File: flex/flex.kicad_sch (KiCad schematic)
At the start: 6 parts, among them SW1 SW_Push, SW2 SW_Push, SW3 SW_Push

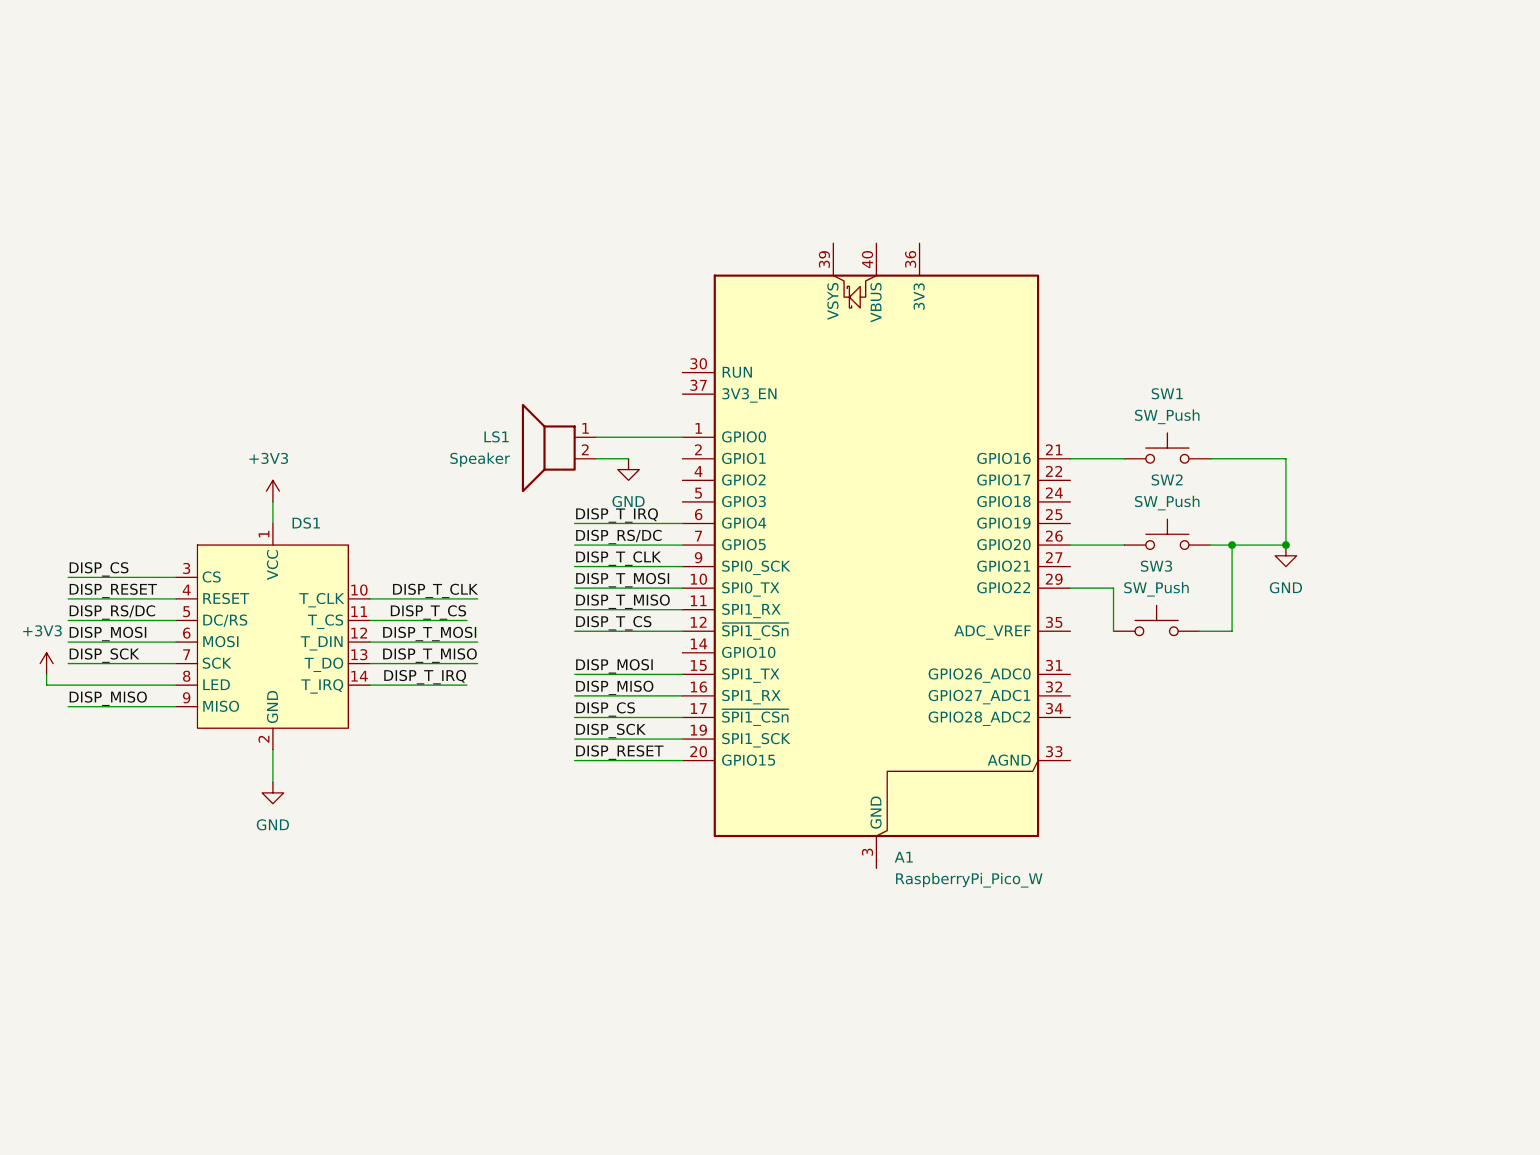
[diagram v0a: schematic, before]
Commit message: added 3d models and moved buttons and edge
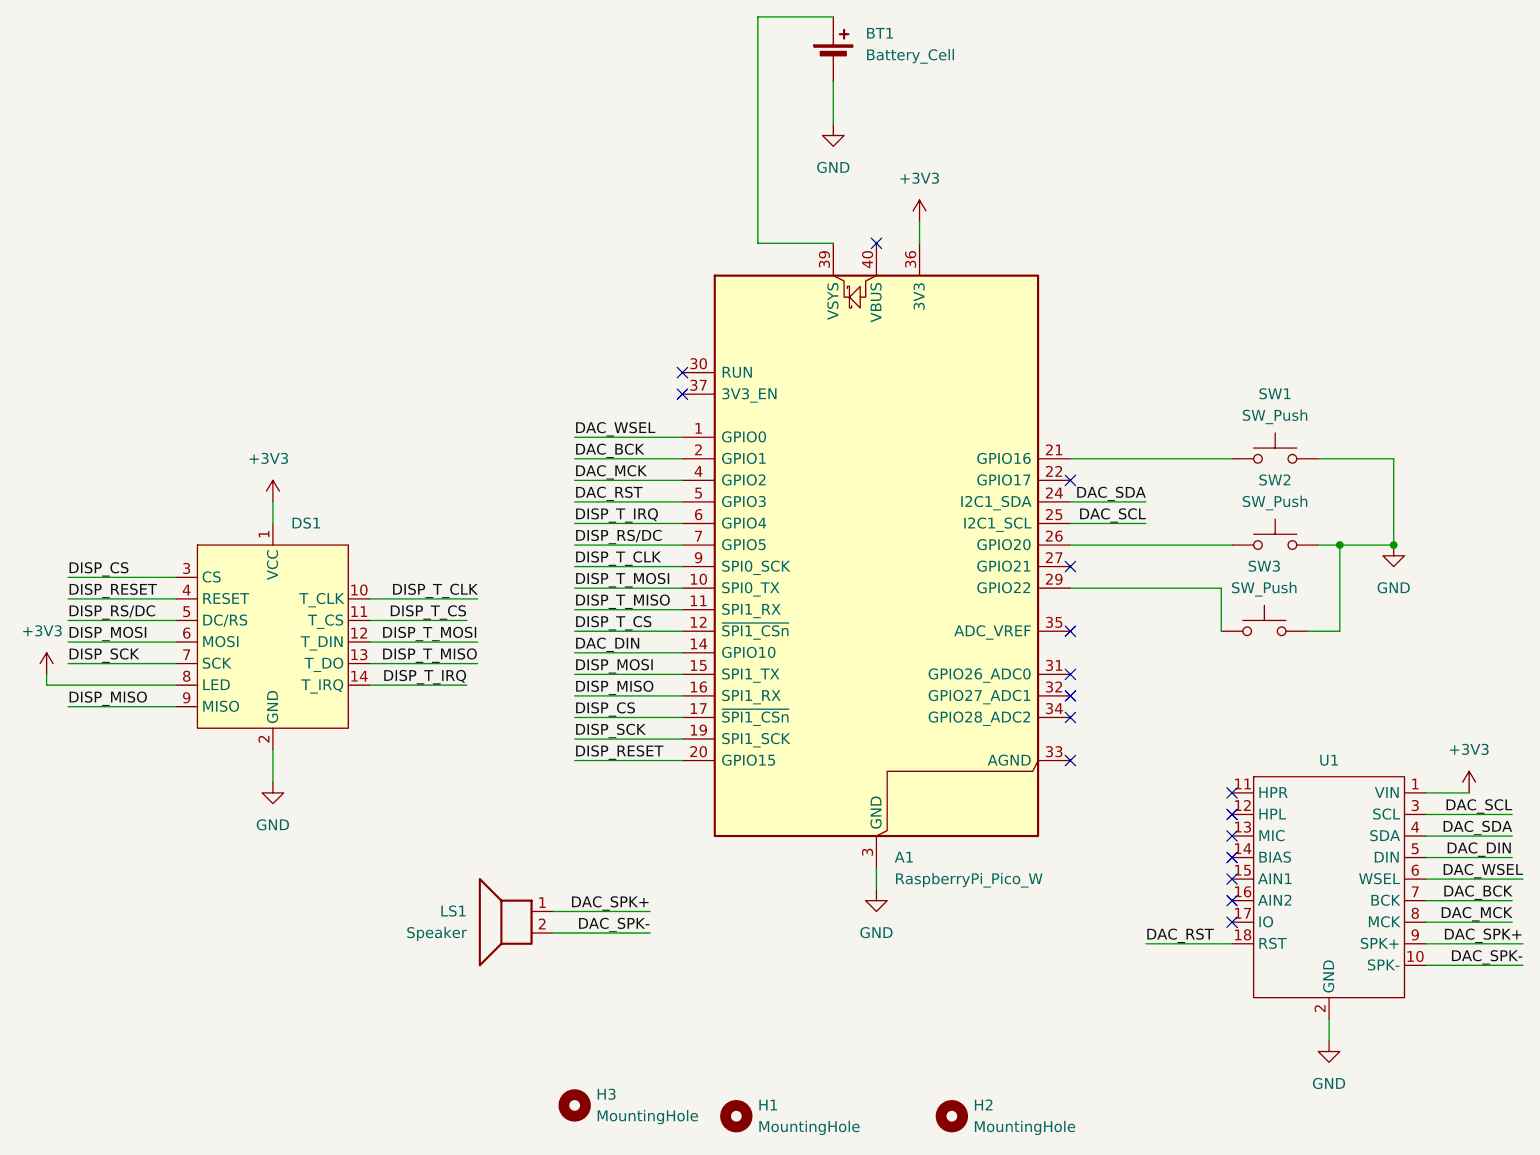
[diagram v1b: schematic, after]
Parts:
- added BT1: Battery_Cell, Connector_PinHeader_2.54mm:PinHeader_1x02_P2.54mm_Vertical, symbol Device:Battery_Cell
- added H1, H2, H3: MountingHole, MountingHole:MountingHole_2.2mm_M2, symbol Mechanical:MountingHole
- added U1: (no value), LIB:DAC, symbol lib:dac
- LS1: footprint (none) -> Connector_PinHeader_2.54mm:PinHeader_1x02_P2.54mm_Vertical
- SW1: footprint (none) -> easyeda2kicad:SW-TH_4P-L4.5-W4.5-P3.00-LS4.8
- SW2, SW3: footprint (none) -> Button_Switch_THT:SW_SPST_Omron_B3F-315x_Angled
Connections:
- net +3V3: now also A1.36 (3V3), U1.1 (VIN)
- net GND: now also A1.13 (GND), A1.18 (GND), A1.23 (GND), A1.28 (GND), A1.3 (GND), A1.38 (GND), A1.8 (GND), BT1.2 (-), U1.2 (GND); no longer LS1.2
- net DAC_SPK+: now reaches LS1.1
- net DAC_SPK+: now also U1.9 (SPK+); no longer A1.1 (GPIO0)
- net DAC_DIN: now reaches A1.14 (GPIO10)
- net DAC_DIN: now also U1.5 (DIN)
- net DAC_BCK: now reaches A1.2 (GPIO1)
- net DAC_BCK: now also U1.7 (BCK)
- net DAC_SDA: now reaches A1.24 (GPIO18)
- net DAC_SDA: now also U1.4 (SDA)
- net DAC_SCL: now reaches A1.25 (GPIO19)
- net DAC_SCL: now also U1.3 (SCL)
- net at A1.39 (VSYS): now also BT1.1 (+)
- net DAC_MCK: now reaches A1.4 (GPIO2)
- net DAC_MCK: now also U1.8 (MCK)
- net DAC_RST: now reaches A1.5 (GPIO3)
- net DAC_RST: now also U1.18 (RST)
- new net DAC_SPK-: LS1.2, U1.10 (SPK-)
- new net DAC_WSEL: A1.1 (GPIO0), U1.6 (WSEL)
- no-connect marks 0 -> 17
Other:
- moved on the sheet: LS1, SW1, SW2, SW3

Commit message: rendered and coded firmware
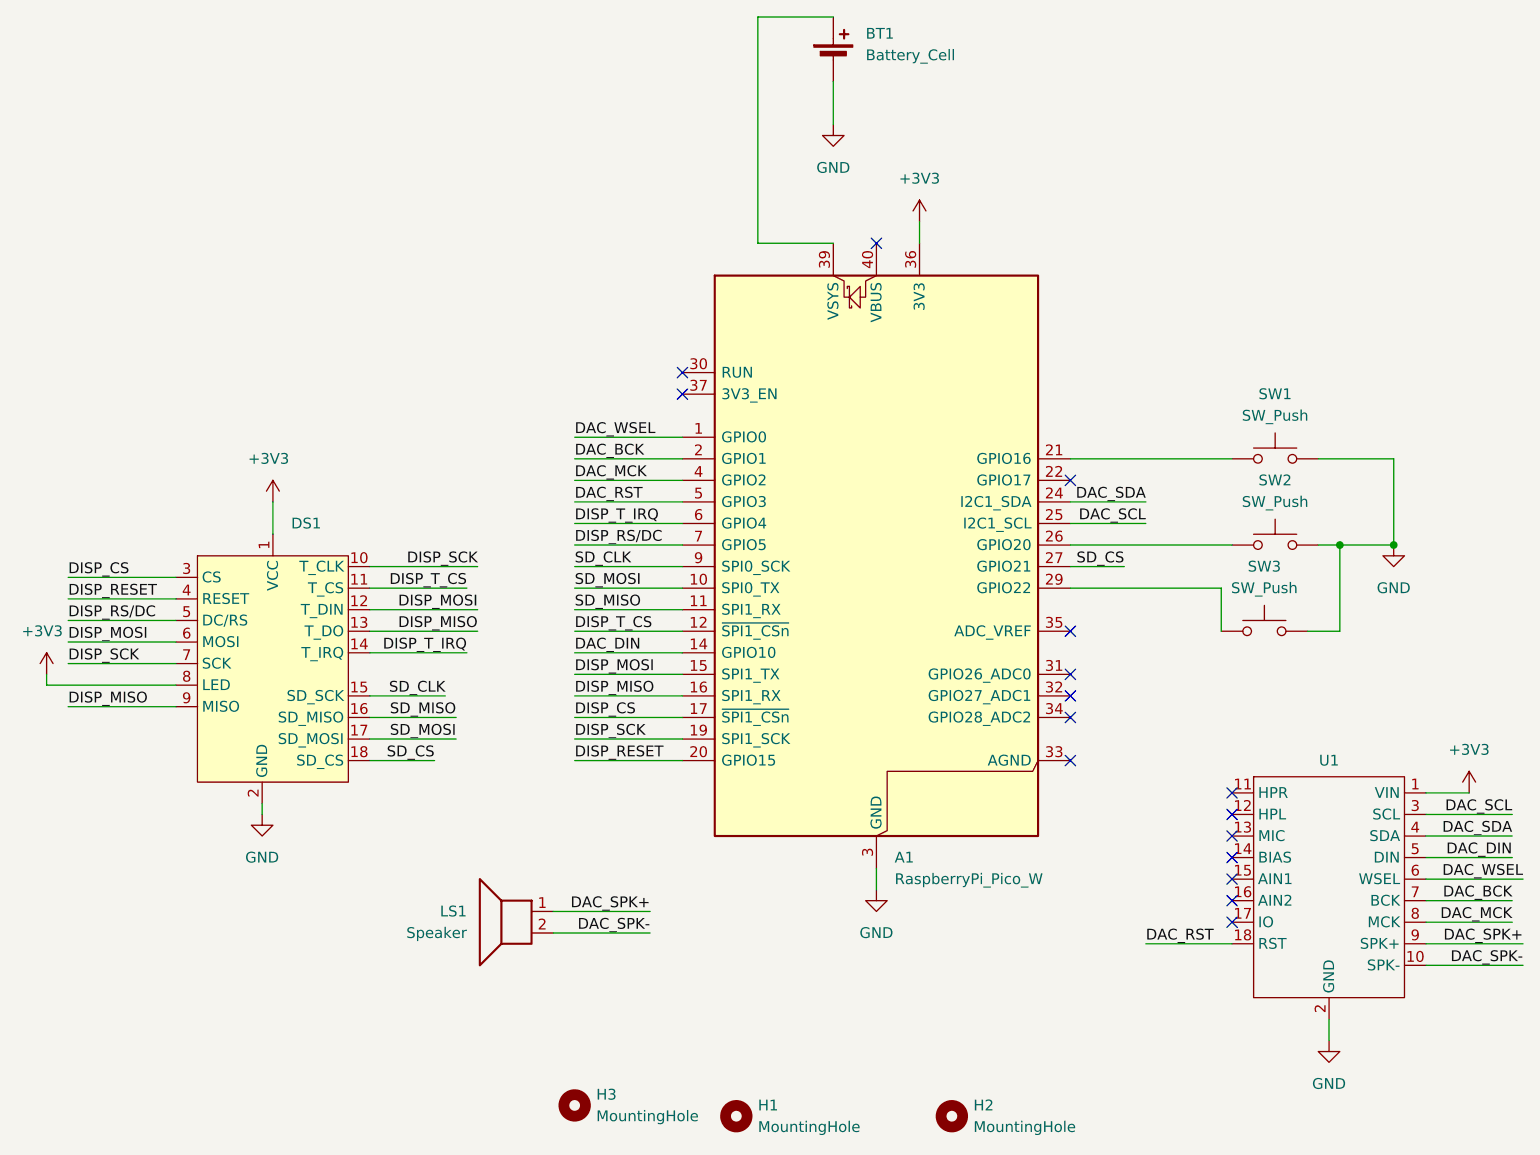
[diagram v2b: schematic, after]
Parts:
- DS1: footprint Connector_PinHeader_2.54mm:PinHeader_1x14_P2.54mm_Vertical -> LIB:Display
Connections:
- net DISP_MISO: now also DS1.13 (T_DO)
- net DISP_MOSI: now also DS1.12 (T_DIN)
- net DISP_SCK: now also DS1.10 (T_CLK)
- net SD_CS: now reaches A1.27 (GPIO21)
- net SD_CS: now also DS1.18 (SD_CS)
- net DISP_T_CLK renamed SD_CLK
- net SD_CLK: now also DS1.15 (SD_SCK); no longer DS1.10 (T_CLK)
- net DISP_T_MISO renamed SD_MISO
- net SD_MISO: now also DS1.16 (SD_MISO); no longer DS1.13 (T_DO)
- net DISP_T_MOSI renamed SD_MOSI
- net SD_MOSI: now also DS1.17 (SD_MOSI); no longer DS1.12 (T_DIN)
- no-connect marks 17 -> 16
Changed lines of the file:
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@@
-	)
-	(no_connect
-		(at 163.83 99.06)
 	)
 	(no_connect
@@
 	(wire
 		(pts
+			(xy 81.28 114.3) (xy 90.17 114.3)
+		)
+		(stroke
+			(width 0)
+			(type default)
+		)
+	)
+	(wire
+		(pts
 			(xy 105.41 114.3) (xy 118.11 114.3)
 		)
@@
 	(wire
 		(pts
+			(xy 81.28 119.38) (xy 91.44 119.38)
+		)
+		(stroke
+			(width 0)
+			(type default)
+		)
+	)
+	(wire
+		(pts
 			(xy 163.83 86.36) (xy 182.88 86.36)
 		)
@@
 	(wire
 		(pts
+			(xy 81.28 116.84) (xy 91.44 116.84)
+		)
+		(stroke
+			(width 0)
+			(type default)
+		)
+	)
+	(wire
+		(pts
 			(xy 195.58 106.68) (xy 195.58 96.52)
 		)
@@
 	(wire
 		(pts
-			(xy 81.28 102.87) (xy 93.98 102.87)
+			(xy 81.28 99.06) (xy 93.98 99.06)
 		)
 		(stroke
@@
 	(wire
 		(pts
+			(xy 68.58 127) (xy 68.58 128.27)
+		)
+		(stroke
+			(width 0)
+			(type default)
+		)
+	)
+	(wire
+		(pts
 			(xy 181.61 101.6) (xy 181.61 106.68)
 		)
@@
 	(wire
 		(pts
-			(xy 81.28 105.41) (xy 92.71 105.41)
-		)
-		(stroke
-			(width 0)
-			(type default)
-		)
-	)
-	(wire
-		(pts
-			(xy 81.28 107.95) (xy 93.98 107.95)
+			(xy 81.28 101.6) (xy 92.71 101.6)
+		)
+		(stroke
+			(width 0)
+			(type default)
+		)
+	)
+	(wire
+		(pts
+			(xy 81.28 104.14) (xy 93.98 104.14)
 		)
 		(stroke
@@
 	(wire
 		(pts
-			(xy 69.85 120.65) (xy 69.85 124.46)
+			(xy 81.28 121.92) (xy 88.9 121.92)
 		)
 		(stroke
@@
 	(wire
 		(pts
+			(xy 69.85 91.44) (xy 69.85 95.25)
+		)
+		(stroke
+			(width 0)
+			(type default)
+		)
+	)
+	(wire
+		(pts
 			(xy 105.41 96.52) (xy 118.11 96.52)
 		)
@@
 	(wire
 		(pts
-			(xy 81.28 113.03) (xy 92.71 113.03)
-		)
-		(stroke
-			(width 0)
-			(type default)
-		)
-	)
-	(wire
-		(pts
-			(xy 69.85 91.44) (xy 69.85 93.98)
+			(xy 163.83 99.06) (xy 170.18 99.06)
+		)
+		(stroke
+			(width 0)
+			(type default)
+		)
+	)
+	(wire
+		(pts
+			(xy 81.28 109.22) (xy 92.71 109.22)
 		)
 		(stroke
@@
 	(wire
 		(pts
-			(xy 81.28 110.49) (xy 93.98 110.49)
+			(xy 81.28 106.68) (xy 93.98 106.68)
 		)
 		(stroke
@@
 		)
 	)
-	(label "DISP_T_MISO"
-		(at 93.98 110.49 180)
+	(label "SD_CS"
+		(at 170.18 99.06 180)
 		(effects
 			(font
@@
 		)
 	)
-	(label "DISP_T_CLK"
-		(at 93.98 102.87 180)
-		(effects
-			(font
-				(size 1.27 1.27)
-			)
-			(justify right bottom)
-		)
-	)
 	(label "DISP_T_IRQ"
 		(at 105.41 93.98 0)
@@
 		)
 	)
+	(label "DISP_MISO"
+		(at 93.98 106.68 180)
+		(effects
+			(font
+				(size 1.27 1.27)
+			)
+			(justify right bottom)
+		)
+	)
 	(label "DAC_RST"
 		(at 172.72 143.51 0)
@@
 		)
 	)
+	(label "DISP_MOSI"
+		(at 93.98 104.14 180)
+		(effects
+			(font
+				(size 1.27 1.27)
+			)
+			(justify right bottom)
+		)
+	)
 	(label "DISP_SCK"
 		(at 45.72 110.49 0)
@@
 		)
 	)
-	(label "DISP_T_CLK"
+	(label "SD_CLK"
 		(at 105.41 99.06 0)
 		(effects
@@
 		)
 	)
-	(label "DISP_T_MOSI"
+	(label "SD_MOSI"
 		(at 105.41 101.6 0)
 		(effects
@@
 		)
 	)
-	(label "DISP_T_MOSI"
-		(at 93.98 107.95 180)
-		(effects
-			(font
-				(size 1.27 1.27)
-			)
-			(justify right bottom)
-		)
-	)
 	(label "DAC_BCK"
 		(at 105.41 86.36 0)
@@
 	)
 	(label "DISP_T_IRQ"
-		(at 92.71 113.03 180)
+		(at 92.71 109.22 180)
 		(effects
 			(font
@@
 		)
 	)
+	(label "SD_CLK"
+		(at 90.17 114.3 180)
+		(effects
+			(font
+				(size 1.27 1.27)
+			)
+			(justify right bottom)
+		)
+	)
 	(label "DAC_RST"
 		(at 105.41 91.44 0)
@@
 		)
 	)
+	(label "SD_CS"
+		(at 88.9 121.92 180)
+		(effects
+			(font
+				(size 1.27 1.27)
+			)
+			(justify right bottom)
+		)
+	)
 	(label "DISP_SCK"
 		(at 105.41 119.38 0)
@@
 		)
 	)
+	(label "DISP_SCK"
+		(at 93.98 99.06 180)
+		(effects
+			(font
+				(size 1.27 1.27)
+			)
+			(justify right bottom)
+		)
+	)
 	(label "DAC_SDA"
 		(at 172.72 91.44 180)
@@
 		)
 	)
-	(label "DISP_T_MISO"
+	(label "SD_MOSI"
+		(at 91.44 119.38 180)
+		(effects
+			(font
+				(size 1.27 1.27)
+			)
+			(justify right bottom)
+		)
+	)
+	(label "SD_MISO"
 		(at 105.41 104.14 0)
 		(effects
@@
 		)
 	)
+	(label "SD_MISO"
+		(at 91.44 116.84 180)
+		(effects
+			(font
+				(size 1.27 1.27)
+			)
+			(justify right bottom)
+		)
+	)
 	(label "DAC_SCL"
 		(at 172.72 93.98 180)
@@
 	)
 	(label "DISP_T_CS"
-		(at 92.71 105.41 180)
+		(at 92.71 101.6 180)
 		(effects
 			(font
@@
 			)
 		)
-		(property "Footprint" "Connector_PinHeader_2.54mm:PinHeader_1x14_P2.54mm_Vertical"
+		(property "Footprint" "LIB:Display"
 			(at 69.85 105.41 0)
 			(hide yes)
@@
 		)
 		(pin "14"
+		)
+		(pin "18"
+		)
+		(pin "15"
+		)
+		(pin "16"
+		)
+		(pin "17"
 		)
 		(instances
@@
 	(symbol
 		(lib_id "power:GND")
-		(at 69.85 124.46 0)
+		(at 68.58 128.27 0)
 		(mirror y)
 		(unit 1)
@@
 		(fields_autoplaced yes)
 		(property "Reference" "#PWR04"
-			(at 69.85 130.81 0)
+			(at 68.58 134.62 0)
 			(hide yes)
 			(show_name no)
@@
 		)
 		(property "Value" "GND"
-			(at 69.85 129.54 0)
+			(at 68.58 133.35 0)
 			(show_name no)
 			(do_not_autoplace no)
@@
 		)
 		(property "Footprint" ""
-			(at 69.85 124.46 0)
+			(at 68.58 128.27 0)
 			(hide yes)
 			(show_name no)
@@
 		)
 		(property "Datasheet" ""
-			(at 69.85 124.46 0)
+			(at 68.58 128.27 0)
 			(hide yes)
 			(show_name no)
@@
 		)
 		(property "Description" "Power symbol creates a global label with name \"GND\" , ground"
-			(at 69.85 124.46 0)
-			(hide yes)
-			(show_name no)
+			(at 68.58 128.27 0)
+			(hide yes)
+			(show_name no)
